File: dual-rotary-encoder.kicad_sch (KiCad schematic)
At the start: 9 parts

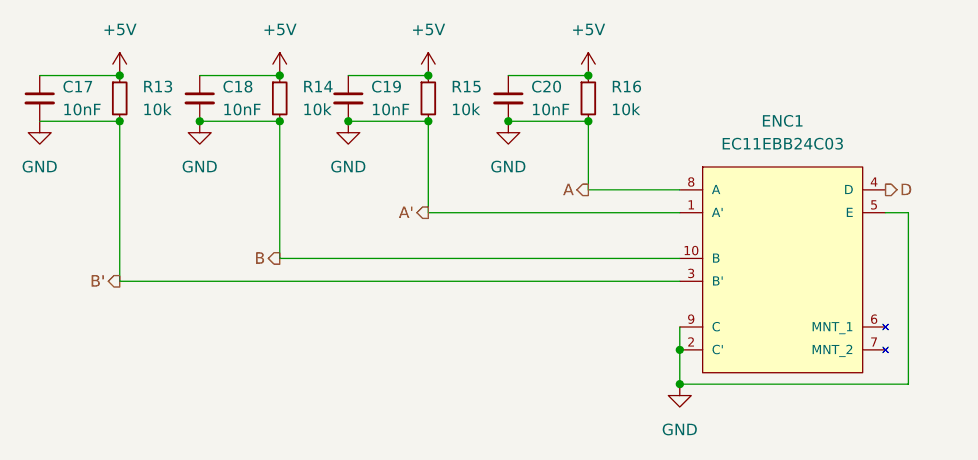
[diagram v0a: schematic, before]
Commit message: Add RP2040
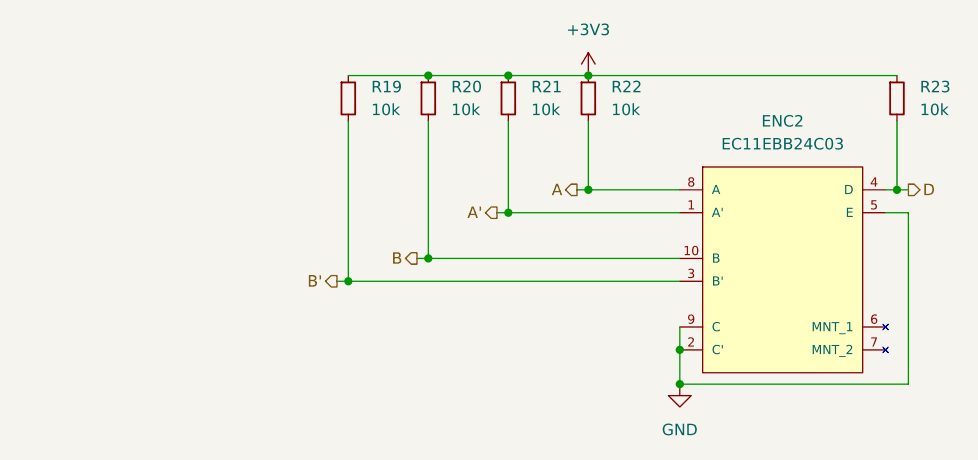
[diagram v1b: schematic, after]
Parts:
- removed C17, C18, C19, C20: 10nF, symbol Device:C_Small
- added R23: 10k, symbol Device:R_Small
- renumbered ENC1 to ENC2, R13 to R19, R14 to R20, R15 to R21, R16 to R22
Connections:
- net D: now also R23.2
- net GND: no longer ENC2.1 (A'), ENC2.10 (B), ENC2.3 (B'), ENC2.8 (A), R19.2, R20.2, R21.2, R22.2
- net +5V renamed +3V3
- net +3V3: now also R23.1
- new net A: ENC2.8 (A), R22.2
- new net A': ENC2.1 (A'), R21.2
- new net B: ENC2.10 (B), R20.2
- new net B': ENC2.3 (B'), R19.2
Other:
- moved on the sheet: R19, R20, R21

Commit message: Bunch more schematic work
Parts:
- ENC2: footprint ALPS-EC11EBB24C03-* -> Generic-radio-stack:ALPS-EC11EBB24C03-0
- R23: renamed from R19; footprint (none) -> Resistor_SMD:R_0805_2012Metric
- R24: renamed from R20; footprint (none) -> Resistor_SMD:R_0805_2012Metric
- R25: renamed from R21; footprint (none) -> Resistor_SMD:R_0805_2012Metric
- R26: renamed from R22; footprint (none) -> Resistor_SMD:R_0805_2012Metric
- R27: renamed from R23; footprint (none) -> Resistor_SMD:R_0805_2012Metric
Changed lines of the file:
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@@
   (symbol (lib_id "Device:R_Small") (at 143.51 69.85 0)
     (in_bom yes) (on_board yes) (fields_autoplaced)
-    (property "Reference" "R23" (id 0) (at 146.05 68.5799 0)
+    (property "Reference" "R27" (id 0) (at 146.05 68.5799 0)
       (effects (font (size 1.27 1.27)) (justify left))
     )
@@
       (effects (font (size 1.27 1.27)) (justify left))
     )
-    (property "Footprint" "" (id 2) (at 143.51 69.85 0)
+    (property "Footprint" "Resistor_SMD:R_0805_2012Metric" (id 2) (at 143.51 69.85 0)
       (effects (font (size 1.27 1.27)) hide)
     )
@@
   (symbol (lib_id "power:+3V3") (at 109.22 67.31 0)
     (in_bom yes) (on_board yes) (fields_autoplaced)
-    (property "Reference" "#PWR?" (id 0) (at 109.22 71.12 0)
+    (property "Reference" "#PWR046" (id 0) (at 109.22 71.12 0)
       (effects (font (size 1.27 1.27)) hide)
     )
@@
   (symbol (lib_id "Device:R_Small") (at 100.33 69.85 0)
     (in_bom yes) (on_board yes) (fields_autoplaced)
-    (property "Reference" "R21" (id 0) (at 102.87 68.5799 0)
+    (property "Reference" "R25" (id 0) (at 102.87 68.5799 0)
       (effects (font (size 1.27 1.27)) (justify left))
     )
@@
       (effects (font (size 1.27 1.27)) (justify left))
     )
-    (property "Footprint" "" (id 2) (at 100.33 69.85 0)
+    (property "Footprint" "Resistor_SMD:R_0805_2012Metric" (id 2) (at 100.33 69.85 0)
       (effects (font (size 1.27 1.27)) hide)
     )
@@
     (property "Reference" "ENC2" (id 0) (at 130.81 72.39 0))
     (property "Value" "EC11EBB24C03" (id 1) (at 130.81 74.93 0))
-    (property "Footprint" "ALPS-EC11EBB24C03-*" (id 2) (at 116.84 69.85 0)
+    (property "Footprint" "Generic-radio-stack:ALPS-EC11EBB24C03-0" (id 2) (at 116.84 69.85 0)
       (effects (font (size 1.27 1.27)) (justify left) hide)
     )
@@
   (symbol (lib_id "power:GND") (at 119.38 101.6 0)
     (in_bom yes) (on_board yes) (fields_autoplaced)
-    (property "Reference" "#PWR045" (id 0) (at 119.38 107.95 0)
+    (property "Reference" "#PWR047" (id 0) (at 119.38 107.95 0)
       (effects (font (size 1.27 1.27)) hide)
     )
@@
   (symbol (lib_id "Device:R_Small") (at 109.22 69.85 0)
     (in_bom yes) (on_board yes) (fields_autoplaced)
-    (property "Reference" "R22" (id 0) (at 111.76 68.5799 0)
+    (property "Reference" "R26" (id 0) (at 111.76 68.5799 0)
       (effects (font (size 1.27 1.27)) (justify left))
     )
@@
       (effects (font (size 1.27 1.27)) (justify left))
     )
-    (property "Footprint" "" (id 2) (at 109.22 69.85 0)
+    (property "Footprint" "Resistor_SMD:R_0805_2012Metric" (id 2) (at 109.22 69.85 0)
       (effects (font (size 1.27 1.27)) hide)
     )
@@
   (symbol (lib_id "Device:R_Small") (at 91.44 69.85 0)
     (in_bom yes) (on_board yes) (fields_autoplaced)
-    (property "Reference" "R20" (id 0) (at 93.98 68.5799 0)
+    (property "Reference" "R24" (id 0) (at 93.98 68.5799 0)
       (effects (font (size 1.27 1.27)) (justify left))
     )
@@
       (effects (font (size 1.27 1.27)) (justify left))
     )
-    (property "Footprint" "" (id 2) (at 91.44 69.85 0)
+    (property "Footprint" "Resistor_SMD:R_0805_2012Metric" (id 2) (at 91.44 69.85 0)
       (effects (font (size 1.27 1.27)) hide)
     )
@@
   (symbol (lib_id "Device:R_Small") (at 82.55 69.85 0)
     (in_bom yes) (on_board yes) (fields_autoplaced)
-    (property "Reference" "R19" (id 0) (at 85.09 68.5799 0)
+    (property "Reference" "R23" (id 0) (at 85.09 68.5799 0)
       (effects (font (size 1.27 1.27)) (justify left))
     )
@@
       (effects (font (size 1.27 1.27)) (justify left))
     )
-    (property "Footprint" "" (id 2) (at 82.55 69.85 0)
+    (property "Footprint" "Resistor_SMD:R_0805_2012Metric" (id 2) (at 82.55 69.85 0)
       (effects (font (size 1.27 1.27)) hide)
     )

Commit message: Add display footprints and models
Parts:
- R23, R24, R25, R26, R27: footprint Resistor_SMD:R_0805_2012Metric -> Generic-radio-stack:Perfect_0402
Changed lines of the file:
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@@
       (effects (font (size 1.27 1.27)) (justify left))
     )
-    (property "Footprint" "Resistor_SMD:R_0805_2012Metric" (id 2) (at 143.51 69.85 0)
+    (property "Footprint" "Generic-radio-stack:Perfect_0402" (id 2) (at 143.51 69.85 0)
       (effects (font (size 1.27 1.27)) hide)
     )
@@
       (effects (font (size 1.27 1.27)) (justify left))
     )
-    (property "Footprint" "Resistor_SMD:R_0805_2012Metric" (id 2) (at 100.33 69.85 0)
+    (property "Footprint" "Generic-radio-stack:Perfect_0402" (id 2) (at 100.33 69.85 0)
       (effects (font (size 1.27 1.27)) hide)
     )
@@
       (effects (font (size 1.27 1.27)) (justify left))
     )
-    (property "Footprint" "Resistor_SMD:R_0805_2012Metric" (id 2) (at 109.22 69.85 0)
+    (property "Footprint" "Generic-radio-stack:Perfect_0402" (id 2) (at 109.22 69.85 0)
       (effects (font (size 1.27 1.27)) hide)
     )
@@
       (effects (font (size 1.27 1.27)) (justify left))
     )
-    (property "Footprint" "Resistor_SMD:R_0805_2012Metric" (id 2) (at 91.44 69.85 0)
+    (property "Footprint" "Generic-radio-stack:Perfect_0402" (id 2) (at 91.44 69.85 0)
       (effects (font (size 1.27 1.27)) hide)
     )
@@
       (effects (font (size 1.27 1.27)) (justify left))
     )
-    (property "Footprint" "Resistor_SMD:R_0805_2012Metric" (id 2) (at 82.55 69.85 0)
+    (property "Footprint" "Generic-radio-stack:Perfect_0402" (id 2) (at 82.55 69.85 0)
       (effects (font (size 1.27 1.27)) hide)
     )
